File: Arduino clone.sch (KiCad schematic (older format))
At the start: 12 parts

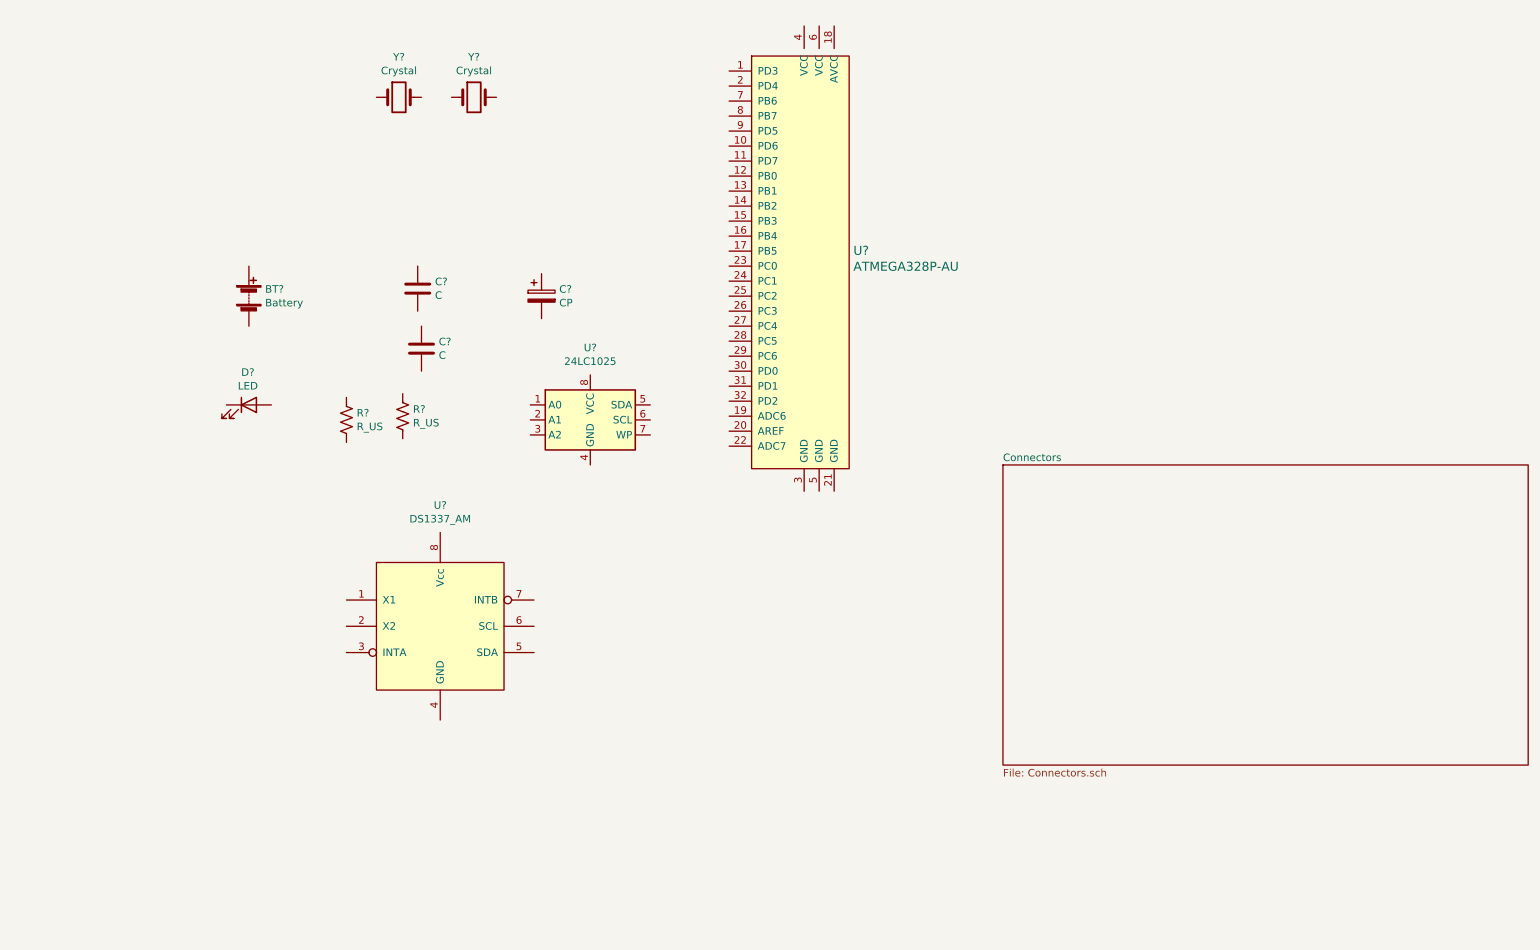
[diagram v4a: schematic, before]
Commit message: Arranged symbols appropriately
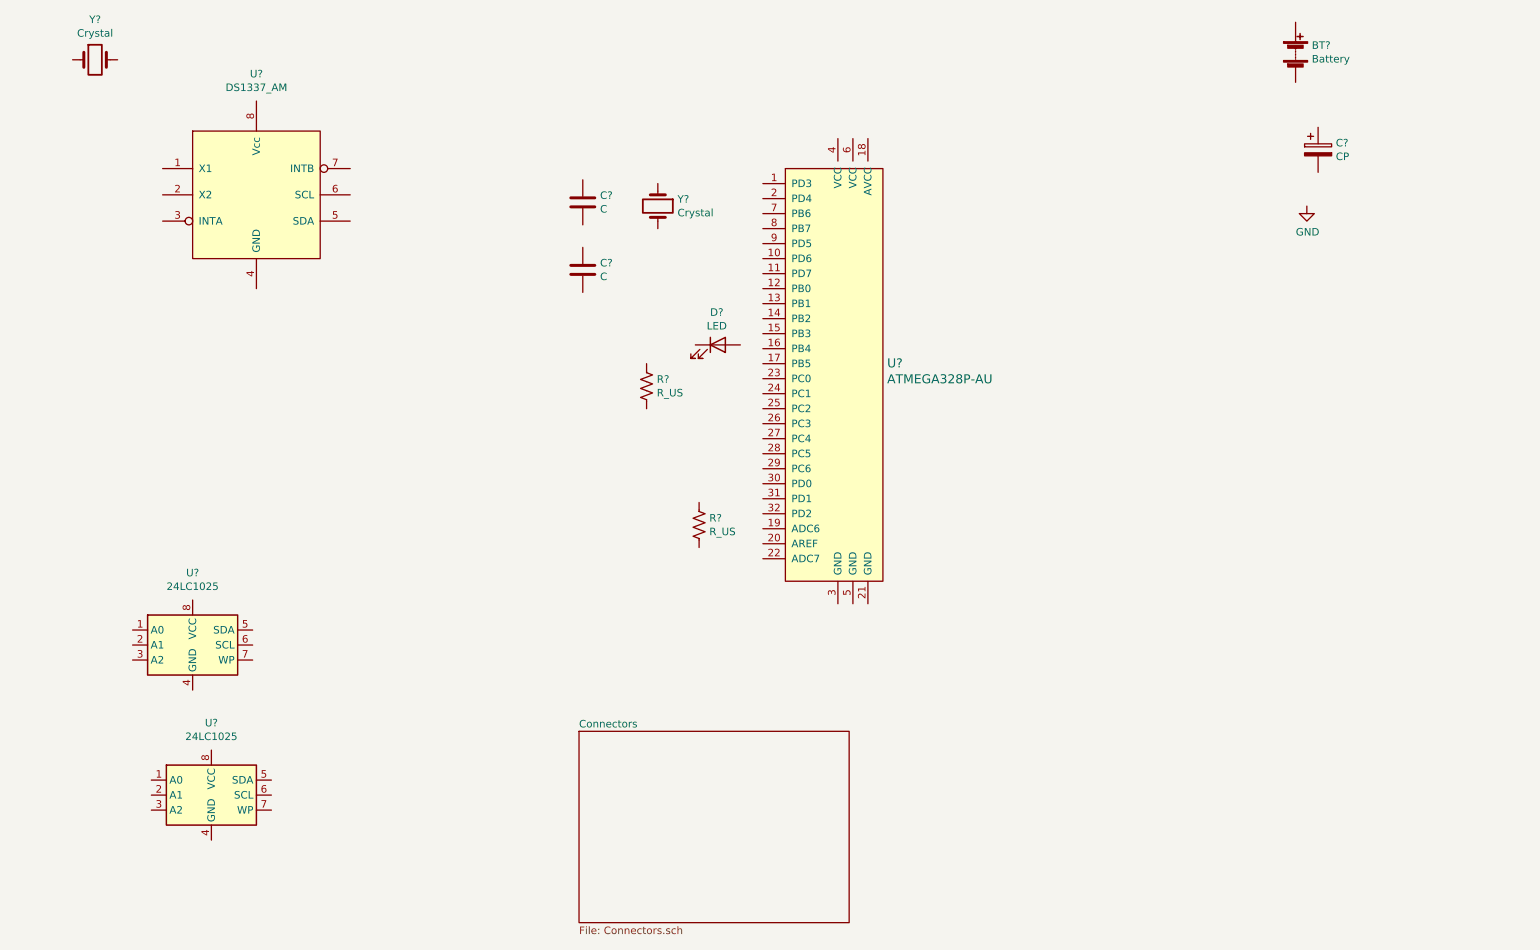
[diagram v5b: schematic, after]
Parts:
- added U?: 24LC1025, symbol Memory_EEPROM:24LC1025
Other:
- moved on the sheet: BT?, C?, D?, R?, U?, Y?
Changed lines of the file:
@@
 L Device:Battery BT?
 U 1 1 601B418E
-P 2475 3125
-F 0 "BT?" H 2583 3171 50  0000 L CNN
-F 1 "Battery" H 2583 3080 50  0000 L CNN
-F 2 "" V 2475 3185 50  0001 C CNN
-F 3 "~" V 2475 3185 50  0001 C CNN
-	1    2475 3125
+P 9450 1500
+F 0 "BT?" H 9558 1546 50  0000 L CNN
+F 1 "Battery" H 9558 1455 50  0000 L CNN
+F 2 "" V 9450 1560 50  0001 C CNN
+F 3 "~" V 9450 1560 50  0001 C CNN
+	1    9450 1500
 	1    0    0    -1
 $EndComp
@@
 L Device:C C?
 U 1 1 601B4C5C
-P 3600 3075
-F 0 "C?" H 3715 3121 50  0000 L CNN
-F 1 "C" H 3715 3030 50  0000 L CNN
-F 2 "" H 3638 2925 50  0001 C CNN
-F 3 "~" H 3600 3075 50  0001 C CNN
-	1    3600 3075
+P 4700 2500
+F 0 "C?" H 4815 2546 50  0000 L CNN
+F 1 "C" H 4815 2455 50  0000 L CNN
+F 2 "" H 4738 2350 50  0001 C CNN
+F 3 "~" H 4700 2500 50  0001 C CNN
+	1    4700 2500
 	1    0    0    -1
 $EndComp
@@
 L Device:C C?
 U 1 1 601B50D6
-P 3625 3475
-F 0 "C?" H 3740 3521 50  0000 L CNN
-F 1 "C" H 3740 3430 50  0000 L CNN
-F 2 "" H 3663 3325 50  0001 C CNN
-F 3 "~" H 3625 3475 50  0001 C CNN
-	1    3625 3475
+P 4700 2950
+F 0 "C?" H 4815 2996 50  0000 L CNN
+F 1 "C" H 4815 2905 50  0000 L CNN
+F 2 "" H 4738 2800 50  0001 C CNN
+F 3 "~" H 4700 2950 50  0001 C CNN
+	1    4700 2950
 	1    0    0    -1
 $EndComp
@@
 L Device:CP C?
 U 1 1 601B5633
-P 4425 3125
-F 0 "C?" H 4543 3171 50  0000 L CNN
-F 1 "CP" H 4543 3080 50  0000 L CNN
-F 2 "" H 4463 2975 50  0001 C CNN
-F 3 "~" H 4425 3125 50  0001 C CNN
-	1    4425 3125
+P 9600 2150
+F 0 "C?" H 9718 2196 50  0000 L CNN
+F 1 "CP" H 9718 2105 50  0000 L CNN
+F 2 "" H 9638 2000 50  0001 C CNN
+F 3 "~" H 9600 2150 50  0001 C CNN
+	1    9600 2150
+	1    0    0    -1
+$EndComp
+$Comp
+L Device:R_US R?
+U 1 1 601B6694
+P 5125 3725
+F 0 "R?" H 5193 3771 50  0000 L CNN
+F 1 "R_US" H 5193 3680 50  0000 L CNN
+F 2 "" V 5165 3715 50  0001 C CNN
+F 3 "~" H 5125 3725 50  0001 C CNN
+	1    5125 3725
+	1    0    0    -1
+$EndComp
+$Comp
+L Device:R_US R?
+U 1 1 601B6C79
+P 5475 4650
+F 0 "R?" H 5543 4696 50  0000 L CNN
+F 1 "R_US" H 5543 4605 50  0000 L CNN
+F 2 "" V 5515 4640 50  0001 C CNN
+F 3 "~" H 5475 4650 50  0001 C CNN
+	1    5475 4650
+	1    0    0    -1
+$EndComp
+$Comp
+L dk_Embedded-Microcontrollers:ATMEGA328P-AU U?
+U 1 1 601BDCDB
+P 6400 3675
+F 0 "U?" H 6728 3778 60  0000 L CNN
+F 1 "ATMEGA328P-AU" H 6728 3672 60  0000 L CNN
+F 2 "digikey-footprints:TQFP-32_7x7mm" H 6600 3875 60  0001 L CNN
+F 3 "http://www.microchip.com/mymicrochip/filehandler.aspx?ddocname=en608326" H 6600 3975 60  0001 L CNN
+F 4 "ATMEGA328P-AU-ND" H 6600 4075 60  0001 L CNN "Digi-Key_PN"
+F 5 "ATMEGA328P-AU" H 6600 4175 60  0001 L CNN "MPN"
+F 6 "Integrated Circuits (ICs)" H 6600 4275 60  0001 L CNN "Category"
+F 7 "Embedded - Microcontrollers" H 6600 4375 60  0001 L CNN "Family"
+F 8 "http://www.microchip.com/mymicrochip/filehandler.aspx?ddocname=en608326" H 6600 4475 60  0001 L CNN "DK_Datasheet_Link"
+F 9 "/product-detail/en/microchip-technology/ATMEGA328P-AU/ATMEGA328P-AU-ND/1832260" H 6600 4575 60  0001 L CNN "DK_Detail_Page"
+F 10 "IC MCU 8BIT 32KB FLASH 32TQFP" H 6600 4675 60  0001 L CNN "Description"
+F 11 "Microchip Technology" H 6600 4775 60  0001 L CNN "Manufacturer"
+F 12 "Active" H 6600 4875 60  0001 L CNN "Status"
+	1    6400 3675
+	1    0    0    -1
+$EndComp
+$Comp
+L Device:Crystal Y?
+U 1 1 601C298C
+P 1450 1550
+F 0 "Y?" H 1450 1818 50  0000 C CNN
+F 1 "Crystal" H 1450 1727 50  0000 C CNN
+F 2 "" H 1450 1550 50  0001 C CNN
+F 3 "~" H 1450 1550 50  0001 C CNN
+	1    1450 1550
+	1    0    0    -1
+$EndComp
+$Comp
+L Device:Crystal Y?
+U 1 1 601C36A9
+P 5200 2525
+F 0 "Y?" V 5154 2656 50  0000 L CNN
+F 1 "Crystal" V 5245 2656 50  0000 L CNN
+F 2 "" H 5200 2525 50  0001 C CNN
+F 3 "~" H 5200 2525 50  0001 C CNN
+	1    5200 2525
+	0    1    1    0
+$EndComp
+$Comp
+L power:GND #PWR?
+U 1 1 601D629C
+P 9525 2525
+F 0 "#PWR?" H 9525 2275 50  0001 C CNN
+F 1 "GND" H 9530 2352 50  0000 C CNN
+F 2 "" H 9525 2525 50  0001 C CNN
+F 3 "" H 9525 2525 50  0001 C CNN
+	1    9525 2525
+	1    0    0    -1
+$EndComp
+$Comp
+L Memory_EEPROM:24LC1025 U?
+U 1 1 601CAEF5
+P 2225 6450
+F 0 "U?" H 2225 6931 50  0000 C CNN
+F 1 "24LC1025" H 2225 6840 50  0000 C CNN
+F 2 "" H 2225 6450 50  0001 C CNN
+F 3 "http://ww1.microchip.com/downloads/en/DeviceDoc/21941B.pdf" H 2225 6450 50  0001 C CNN
+	1    2225 6450
+	1    0    0    -1
+$EndComp
+$Comp
+L Abtahi's_Library:DS1337_AM U?
+U 1 1 601C4304
+P 2525 2450
+F 0 "U?" H 2525 3256 50  0000 C CNN
+F 1 "DS1337_AM" H 2525 3165 50  0000 C CNN
+F 2 "" H 2525 2450 50  0001 C CNN
+F 3 "" H 2525 2450 50  0001 C CNN
+	1    2525 2450
+	1    0    0    -1
+$EndComp
+$Comp
+L Memory_EEPROM:24LC1025 U?
+U 1 1 601B7371
+P 2100 5450
+F 0 "U?" H 2100 5931 50  0000 C CNN
+F 1 "24LC1025" H 2100 5840 50  0000 C CNN
+F 2 "" H 2100 5450 50  0001 C CNN
+F 3 "http://ww1.microchip.com/downloads/en/DeviceDoc/21941B.pdf" H 2100 5450 50  0001 C CNN
+	1    2100 5450
 	1    0    0    -1
 $EndComp
@@
 L Device:LED D?
 U 1 1 601B5CCB
-P 2475 3850
-F 0 "D?" H 2468 4067 50  0000 C CNN
-F 1 "LED" H 2468 3976 50  0000 C CNN
-F 2 "" H 2475 3850 50  0001 C CNN
-F 3 "~" H 2475 3850 50  0001 C CNN
-	1    2475 3850
-	1    0    0    -1
-$EndComp
-$Comp
-L Device:R_US R?
-U 1 1 601B6694
-P 3125 3950
-F 0 "R?" H 3193 3996 50  0000 L CNN
-F 1 "R_US" H 3193 3905 50  0000 L CNN
-F 2 "" V 3165 3940 50  0001 C CNN
-F 3 "~" H 3125 3950 50  0001 C CNN
-	1    3125 3950
-	1    0    0    -1
-$EndComp
-$Comp
-L Device:R_US R?
-U 1 1 601B6C79
-P 3500 3925
-F 0 "R?" H 3568 3971 50  0000 L CNN
-F 1 "R_US" H 3568 3880 50  0000 L CNN
-F 2 "" V 3540 3915 50  0001 C CNN
-F 3 "~" H 3500 3925 50  0001 C CNN
-	1    3500 3925
-	1    0    0    -1
-$EndComp
-$Comp
-L Memory_EEPROM:24LC1025 U?
-U 1 1 601B7371
-P 4750 3950
-F 0 "U?" H 4750 4431 50  0000 C CNN
-F 1 "24LC1025" H 4750 4340 50  0000 C CNN
-F 2 "" H 4750 3950 50  0001 C CNN
-F 3 "http://ww1.microchip.com/downloads/en/DeviceDoc/21941B.pdf" H 4750 3950 50  0001 C CNN
-	1    4750 3950
+P 5600 3450
+F 0 "D?" H 5593 3667 50  0000 C CNN
+F 1 "LED" H 5593 3576 50  0000 C CNN
+F 2 "" H 5600 3450 50  0001 C CNN
+F 3 "~" H 5600 3450 50  0001 C CNN
+	1    5600 3450
 	1    0    0    -1
 $EndComp
 $Sheet
-S 7500 4250 3500 2000
+S 4675 6025 1800 1275
 U 601B8BF2
 F0 "Connectors" 50
 F1 "Connectors.sch" 50
 $EndSheet
-$Comp
-L dk_Embedded-Microcontrollers:ATMEGA328P-AU U?
-U 1 1 601BDCDB
-P 6175 2925
-F 0 "U?" H 6503 3028 60  0000 L CNN
-F 1 "ATMEGA328P-AU" H 6503 2922 60  0000 L CNN
-F 2 "digikey-footprints:TQFP-32_7x7mm" H 6375 3125 60  0001 L CNN
-F 3 "http://www.microchip.com/mymicrochip/filehandler.aspx?ddocname=en608326" H 6375 3225 60  0001 L CNN
-F 4 "ATMEGA328P-AU-ND" H 6375 3325 60  0001 L CNN "Digi-Key_PN"
-F 5 "ATMEGA328P-AU" H 6375 3425 60  0001 L CNN "MPN"
-F 6 "Integrated Circuits (ICs)" H 6375 3525 60  0001 L CNN "Category"
-F 7 "Embedded - Microcontrollers" H 6375 3625 60  0001 L CNN "Family"
-F 8 "http://www.microchip.com/mymicrochip/filehandler.aspx?ddocname=en608326" H 6375 3725 60  0001 L CNN "DK_Datasheet_Link"
-F 9 "/product-detail/en/microchip-technology/ATMEGA328P-AU/ATMEGA328P-AU-ND/1832260" H 6375 3825 60  0001 L CNN "DK_Detail_Page"
-F 10 "IC MCU 8BIT 32KB FLASH 32TQFP" H 6375 3925 60  0001 L CNN "Description"
-F 11 "Microchip Technology" H 6375 4025 60  0001 L CNN "Manufacturer"
-F 12 "Active" H 6375 4125 60  0001 L CNN "Status"
-	1    6175 2925
-	1    0    0    -1
-$EndComp
-$Comp
-L Device:Crystal Y?
-U 1 1 601C298C
-P 3475 1800
-F 0 "Y?" H 3475 2068 50  0000 C CNN
-F 1 "Crystal" H 3475 1977 50  0000 C CNN
-F 2 "" H 3475 1800 50  0001 C CNN
-F 3 "~" H 3475 1800 50  0001 C CNN
-	1    3475 1800
-	1    0    0    -1
-$EndComp
-$Comp
-L Device:Crystal Y?
-U 1 1 601C36A9
-P 3975 1800
-F 0 "Y?" H 3975 2068 50  0000 C CNN
-F 1 "Crystal" H 3975 1977 50  0000 C CNN
-F 2 "" H 3975 1800 50  0001 C CNN
-F 3 "~" H 3975 1800 50  0001 C CNN
-	1    3975 1800
-	1    0    0    -1
-$EndComp
-$Comp
-L Abtahi's_Library:DS1337_AM U?
-U 1 1 601C4304
-P 3750 5325
-F 0 "U?" H 3750 6131 50  0000 C CNN
-F 1 "DS1337_AM" H 3750 6040 50  0000 C CNN
-F 2 "" H 3750 5325 50  0001 C CNN
-F 3 "" H 3750 5325 50  0001 C CNN
-	1    3750 5325
-	1    0    0    -1
-$EndComp
 $EndSCHEMATC

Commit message: Annotated symbols
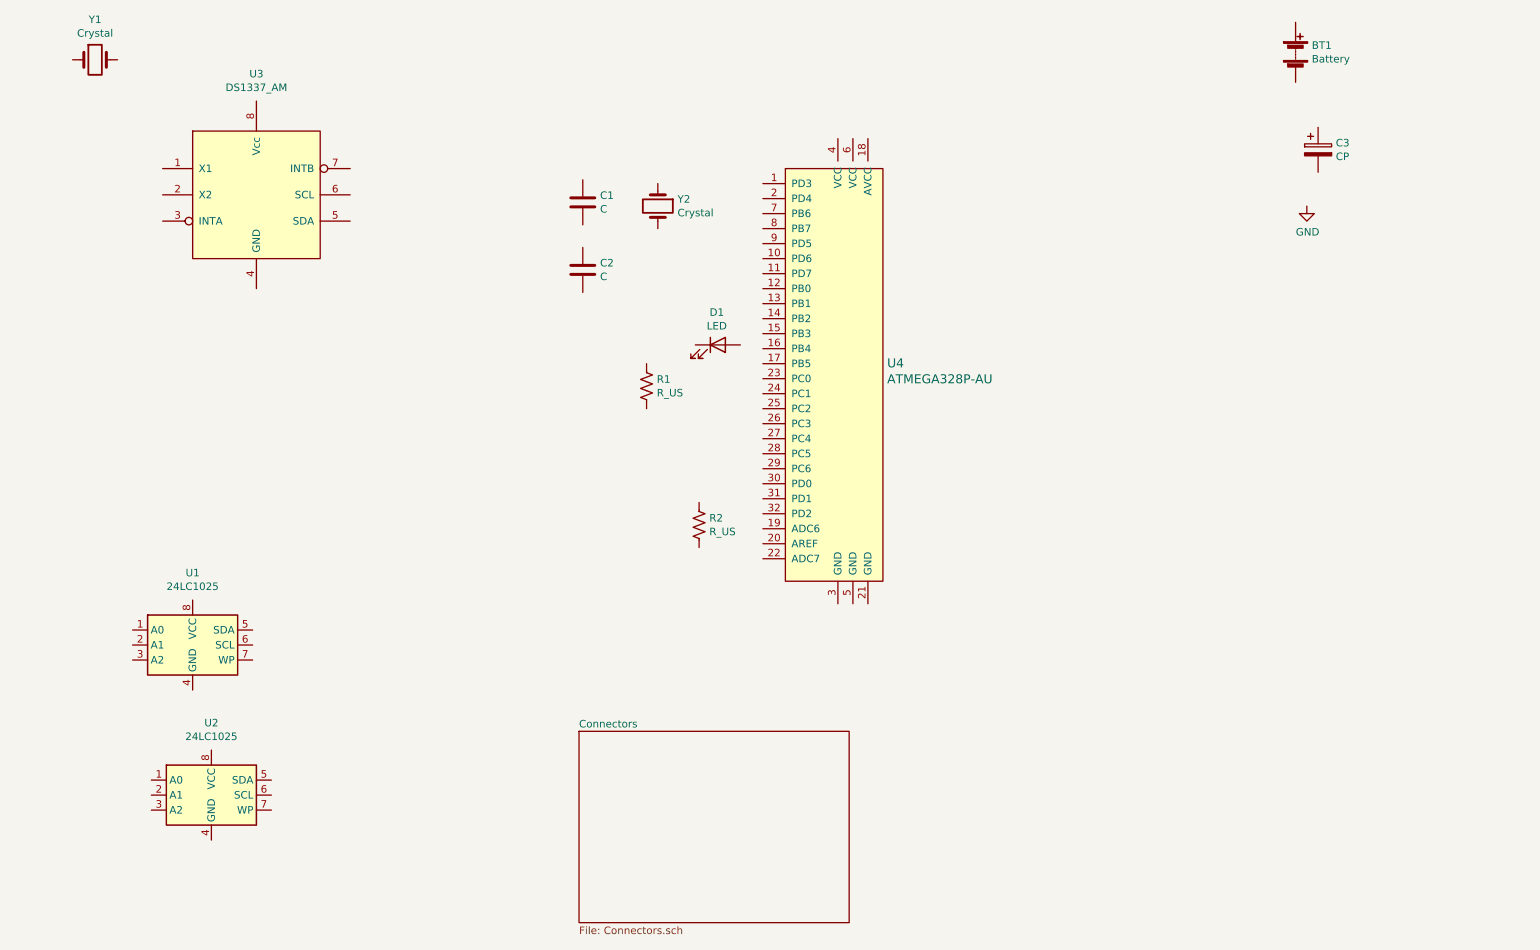
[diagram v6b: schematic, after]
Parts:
- gave numbers to parts that had none: 13
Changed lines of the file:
@@
 $EndDescr
 $Comp
-L Device:Battery BT?
+L Device:Battery BT1
 U 1 1 601B418E
 P 9450 1500
-F 0 "BT?" H 9558 1546 50  0000 L CNN
+F 0 "BT1" H 9558 1546 50  0000 L CNN
 F 1 "Battery" H 9558 1455 50  0000 L CNN
 F 2 "" V 9450 1560 50  0001 C CNN
@@
 $EndComp
 $Comp
-L Device:C C?
+L Device:C C1
 U 1 1 601B4C5C
 P 4700 2500
-F 0 "C?" H 4815 2546 50  0000 L CNN
+F 0 "C1" H 4815 2546 50  0000 L CNN
 F 1 "C" H 4815 2455 50  0000 L CNN
 F 2 "" H 4738 2350 50  0001 C CNN
@@
 $EndComp
 $Comp
-L Device:C C?
+L Device:C C2
 U 1 1 601B50D6
 P 4700 2950
-F 0 "C?" H 4815 2996 50  0000 L CNN
+F 0 "C2" H 4815 2996 50  0000 L CNN
 F 1 "C" H 4815 2905 50  0000 L CNN
 F 2 "" H 4738 2800 50  0001 C CNN
@@
 $EndComp
 $Comp
-L Device:CP C?
+L Device:CP C3
 U 1 1 601B5633
 P 9600 2150
-F 0 "C?" H 9718 2196 50  0000 L CNN
+F 0 "C3" H 9718 2196 50  0000 L CNN
 F 1 "CP" H 9718 2105 50  0000 L CNN
 F 2 "" H 9638 2000 50  0001 C CNN
@@
 $EndComp
 $Comp
-L Device:R_US R?
+L Device:R_US R1
 U 1 1 601B6694
 P 5125 3725
-F 0 "R?" H 5193 3771 50  0000 L CNN
+F 0 "R1" H 5193 3771 50  0000 L CNN
 F 1 "R_US" H 5193 3680 50  0000 L CNN
 F 2 "" V 5165 3715 50  0001 C CNN
@@
 $EndComp
 $Comp
-L Device:R_US R?
+L Device:R_US R2
 U 1 1 601B6C79
 P 5475 4650
-F 0 "R?" H 5543 4696 50  0000 L CNN
+F 0 "R2" H 5543 4696 50  0000 L CNN
 F 1 "R_US" H 5543 4605 50  0000 L CNN
 F 2 "" V 5515 4640 50  0001 C CNN
@@
 $EndComp
 $Comp
-L dk_Embedded-Microcontrollers:ATMEGA328P-AU U?
+L dk_Embedded-Microcontrollers:ATMEGA328P-AU U4
 U 1 1 601BDCDB
 P 6400 3675
-F 0 "U?" H 6728 3778 60  0000 L CNN
+F 0 "U4" H 6728 3778 60  0000 L CNN
 F 1 "ATMEGA328P-AU" H 6728 3672 60  0000 L CNN
 F 2 "digikey-footprints:TQFP-32_7x7mm" H 6600 3875 60  0001 L CNN
@@
 $EndComp
 $Comp
-L Device:Crystal Y?
+L Device:Crystal Y1
 U 1 1 601C298C
 P 1450 1550
-F 0 "Y?" H 1450 1818 50  0000 C CNN
+F 0 "Y1" H 1450 1818 50  0000 C CNN
 F 1 "Crystal" H 1450 1727 50  0000 C CNN
 F 2 "" H 1450 1550 50  0001 C CNN
@@
 $EndComp
 $Comp
-L Device:Crystal Y?
+L Device:Crystal Y2
 U 1 1 601C36A9
 P 5200 2525
-F 0 "Y?" V 5154 2656 50  0000 L CNN
+F 0 "Y2" V 5154 2656 50  0000 L CNN
 F 1 "Crystal" V 5245 2656 50  0000 L CNN
 F 2 "" H 5200 2525 50  0001 C CNN
@@
 $EndComp
 $Comp
-L power:GND #PWR?
+L power:GND #PWR01
 U 1 1 601D629C
 P 9525 2525
-F 0 "#PWR?" H 9525 2275 50  0001 C CNN
+F 0 "#PWR01" H 9525 2275 50  0001 C CNN
 F 1 "GND" H 9530 2352 50  0000 C CNN
 F 2 "" H 9525 2525 50  0001 C CNN
@@
 $EndComp
 $Comp
-L Memory_EEPROM:24LC1025 U?
+L Memory_EEPROM:24LC1025 U2
 U 1 1 601CAEF5
 P 2225 6450
-F 0 "U?" H 2225 6931 50  0000 C CNN
+F 0 "U2" H 2225 6931 50  0000 C CNN
 F 1 "24LC1025" H 2225 6840 50  0000 C CNN
 F 2 "" H 2225 6450 50  0001 C CNN
@@
 $EndComp
 $Comp
-L Abtahi's_Library:DS1337_AM U?
+L Abtahi's_Library:DS1337_AM U3
 U 1 1 601C4304
 P 2525 2450
-F 0 "U?" H 2525 3256 50  0000 C CNN
+F 0 "U3" H 2525 3256 50  0000 C CNN
 F 1 "DS1337_AM" H 2525 3165 50  0000 C CNN
 F 2 "" H 2525 2450 50  0001 C CNN
@@
 $EndComp
 $Comp
-L Memory_EEPROM:24LC1025 U?
+L Memory_EEPROM:24LC1025 U1
 U 1 1 601B7371
 P 2100 5450
-F 0 "U?" H 2100 5931 50  0000 C CNN
+F 0 "U1" H 2100 5931 50  0000 C CNN
 F 1 "24LC1025" H 2100 5840 50  0000 C CNN
 F 2 "" H 2100 5450 50  0001 C CNN
@@
 $EndComp
 $Comp
-L Device:LED D?
+L Device:LED D1
 U 1 1 601B5CCB
 P 5600 3450
-F 0 "D?" H 5593 3667 50  0000 C CNN
+F 0 "D1" H 5593 3667 50  0000 C CNN
 F 1 "LED" H 5593 3576 50  0000 C CNN
 F 2 "" H 5600 3450 50  0001 C CNN
